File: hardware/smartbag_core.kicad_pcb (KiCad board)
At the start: 4 copper layers, 196 x 20 mm, 111 parts, among them J1 FFC optics, 12 way, J2 LiPo 3.7V 2000mAh + NTC, J3 Qi RX coil, J4 FFC FSR matrix, 24 way, J5 SWD debug, Q1 SI2302CDS-T1-GE3, U1 nRF54L15-QFAA-R, U11 BQ51013BRHLR, U2 Acconeer A121, U3 nPM1300-QEAA-R7, U4 BMI270, U5 DRV5032FBDBZR, U6 Acconeer A121, U7 CD74HC4067SM96, U8 TLV9064IPWR, U9 TLV9064IPWR, Y1 32 MHz Cl=8pF, Y2 24 MHz, Y3 24 MHz, Y4 32.768 kHz Cl=9pF

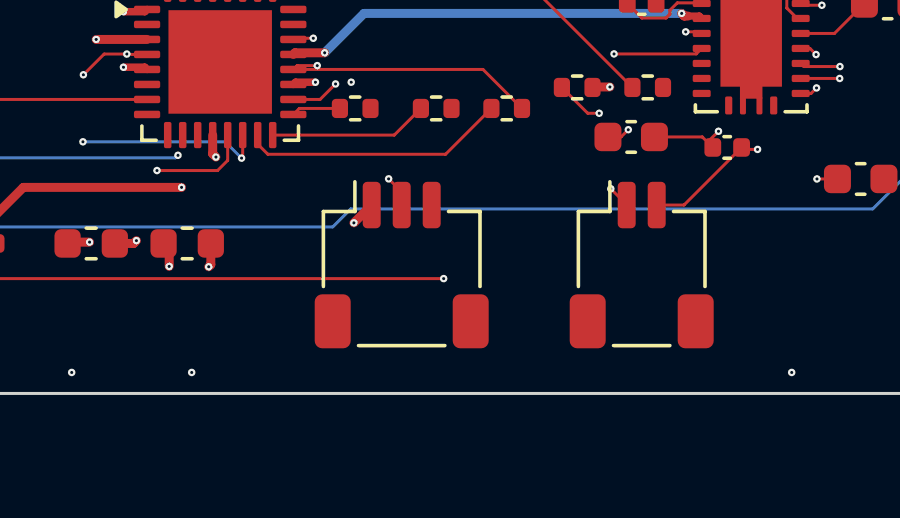
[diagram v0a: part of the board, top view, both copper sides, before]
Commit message: A battery you can order, and the coil comes out from under it
BT1 was the one line in the bill of materials that was not a part: a
4.2 x 58 x 148 mm semi-custom pouch, a shape derived from the insert
floor it had to fill. Nobody stocks that, so the design ended at "have a
cell made".

It is now Jauch LP523450JU — 950 mAh, 53.0 x 34.5 x 5.4 mm (5.8 after
cycling, and the pocket is cut to that), PCM, UN38.3, IEC62133-2, 507 in
stock at Digi-Key for $11.71. It brings its own 10k B=3435 thermistor on
pin 3 of a JST PHR-3 harness, which is exactly what nPM1300 wants and
what firmware/sb_power.c has been written against since the thermal
analysis asked for it.

⛔ AND THE PIN ORDER WAS WRONG. J2 was +, NTC, − — the order you choose
when you are drawing a connector rather than plugging one in. The harness
is 1 red (+), 2 black (−), 3 yellow (NTC), so the real cell would have
put its negative on the PMIC's thermistor input. Nothing here could have
caught it: every check asks whether a net reaches the pins it should, and
none of them knew what colour wire comes out of a pack that did not
exist. J2 is also a PH now rather than an SH — 2 A a contact instead of
1 A, which the note in bom.py had been asking for since the charge
current was first written down, and which is the housing the harness
comes with anyway.

⭐ THE CELL BEING 53 mm INSTEAD OF 148 DISSOLVED THE THERMAL FINDING.
thermal/budget.py has printed a cell near 60 °C against a 45 °C limit on
every run since it was written, and that number rested entirely on one
sentence in its docstring: the Qi coil sits directly under the LiPo. It
did, because a cell that filled the floor left nowhere else for the coil
to be. Now they sit side by side, 62 mm apart, and the heat would have to
cross 4493 K/W of foam to reach the cell when 23 K/W of air sits right
above the coil:

  cell   ~60 °C -> ~26 °C   (0.5% of the coil's rise)
  coil   ~60 °C, unchanged, and now the headline

⚠️ The finding moves rather than disappearing. A watt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
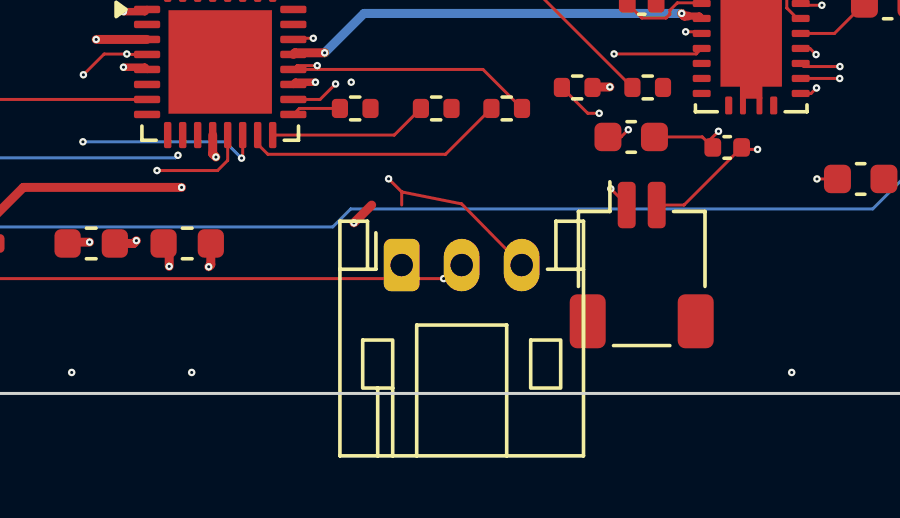
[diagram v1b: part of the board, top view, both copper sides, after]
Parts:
- J2: value LiPo 3.7V 2000mAh + NTC -> Jauch LP523450JU 950mAh; footprint Connector_JST:JST_SH_SM03B-SRSS-TB_1x03-1MP_P1.00mm_Horizontal -> Connector_JST:JST_PH_S3B-PH-K_1x03_P2.00mm_Horizontal
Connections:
- J2 pad 2: NTC -> GND
- J2 pad 3: GND -> NTC
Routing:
- net NTC: track 6.57 -> 11.5 mm

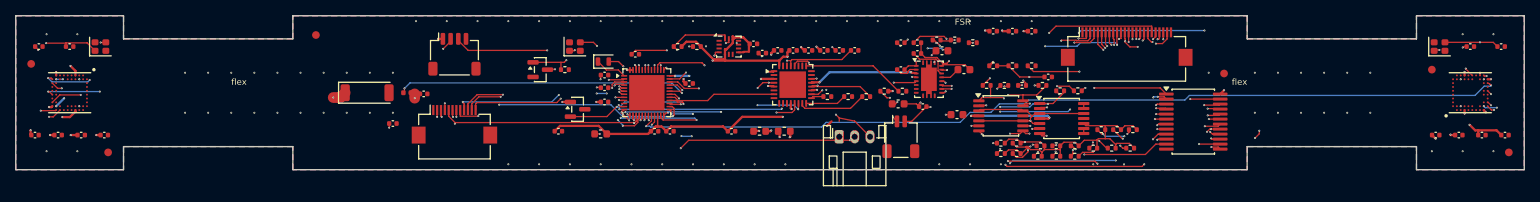
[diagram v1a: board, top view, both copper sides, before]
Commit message: set -e was decoration: every step was piped to tail
A crash inside specctra.py printed its traceback and the pipeline carried
straight on into fill, stitch and route. The board came out with 117
unconnected pads out of an import that had never happened, and reported
it as a normal run.

The cause is one line per script: `python3 ... | tail -1`. A pipeline's
exit status is the LAST command's, tail always succeeds, and `set -e`
therefore never saw anything fail. Five scripts now set pipefail.

⛔ AND THE CRASH ITSELF WAS TWO CLEANUP PASSES ON ONE BOARD. pcbnew's
GetTracks() is a live wrapper: once anything has been removed, it comes
back as a raw SWIG pointer that will not iterate — and on this machine
the second pass segfaulted rather than raising. Both cleanups now decide
against ONE snapshot and the caller removes once. That is not tidiness,
it is the only order that works.

The new cleanup is worth having on its own. Freerouting's optimiser
splits polylines and rounds the joins, leaving segments 0.0001 mm long —
a tenth of a micron — sitting at corners. Nine clearance violations on an
otherwise clean board were pairs of (a real track, one of those), because
a sliver still carries a full track width and so still has a clearance
envelope, pointing wherever the rounding chose.

⚠️ The threshold is 5 um and the number that justifies it is the track
WIDTH, not the fabricator's resolution: the narrowest track here is
100 um, so a 5 um segment lies entirely inside the copper it joins at
either end, twenty times over. Removing it cannot disconnect anything.
The first attempt used 1 um and left a 1.6 um stub behind, which DRC then
reported like any other track.

maze.py can now rip up as well as add. A board that came back with two
tracks 0.127 mm apart where the Power class asks for 0.15 was one it had
nothing to say about — it could only add copper, so it refused its own
routes for making a bad number worse and stopped. It now deletes the
shorter track of each clearance p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
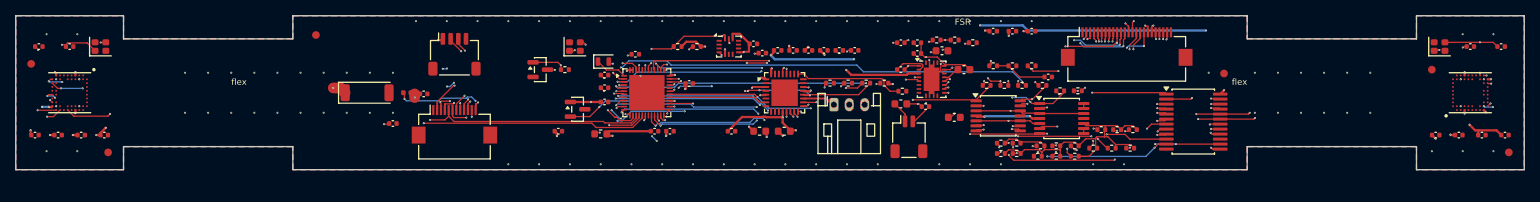
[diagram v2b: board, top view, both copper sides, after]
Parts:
- moved J2 4.23 mm to (218.3, 149.6)
- moved R2 1.78 mm to (217.8, 146.8)
- moved R3 1.75 mm to (220.2, 146.8)
- moved R4 1.75 mm to (222.5, 146.8)
- moved U3 1.48 mm to (211.9, 148.0)
- moved J3 1.05 mm to (228.1, 153.7)
- moved R5 1.05 mm to (224.8, 146.8)
- moved C88 0.49 mm to (233.9, 151.2)
- moved C80 0.35 mm to (227.0, 149.4)
- moved C81 0.35 mm to (230.2, 149.8)
- moved U11 0.35 mm to (231.0, 146.2)
- moved U8 0.35 mm to (239.7, 151.0)
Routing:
- net SPI_MISO: track 204.7 -> 80.8 mm, vias 8 -> 3
- net SPI_MOSI: track 211.5 -> 91.4 mm, vias 5 -> 4
- net MUX_EN_N: track 78.9 -> 0.00 mm, vias 2 -> 0
- net RADAR_EN: track 120.3 -> 77.0 mm, vias 6 -> 2
- net I2C_SCL: track 61.9 -> 80.9 mm, vias 8 -> 7
- net FSR_C7: track 24.2 -> 41.8 mm, vias 4 -> 3
- net FSR_C11: track 36.9 -> 53.0 mm, vias 3 -> 4
- net ADC0: track 62.8 -> 52.1 mm, vias 2 -> 3
- net XTAL32M_1: track 29.8 -> 19.1 mm
- net DECRF: track 19.6 -> 9.56 mm
- net VDD_1V8: track 253.4 -> 243.6 mm, vias 19 -> 21
- net CS_RADAR_L: track 76.0 -> 84.9 mm, vias 3 -> 4
- net FSR_C12: track 42.3 -> 51.2 mm, vias 3 -> 4
- net SWDIO: track 48.6 -> 39.8 mm, vias 3 -> 2
- net FSR_R1: track 32.3 -> 40.2 mm, vias 3 -> 4
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
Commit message: Fourteen ground balls per radar had no via
via_in_pad() dropped a via on every interior ball of the A121 except the
ground ones, and the reasoning for the exception was that ground reaches
the pour. An interior ball cannot reach the pour — that is the whole
argument the function's own docstring makes for the signal balls — and it
does not become able to because of what it is called.

Fourteen of each radar's interior balls are ground. Not one had a via:
the die's ground was tied to the plane by whatever copper squeezed
between balls on a 0.5 mm pitch. On a 60 GHz part with the antenna inside
the package, that is not a cosmetic complaint.

⚠️ IT COST ROUTING AND THE TRADE IS STILL RIGHT. Twenty-eight more vias
in the tightest area of the board, and freerouting came back with three
shorts and four clearance violations where it had had none. Together with
the JST PH the real cell brings — nearly twice the SH's area, in the part
of the board the SPI bus to the right radar has to cross — unconnected
went 3 -> 10 of about 500.

maze.py can now rip vias, not only tracks. The last violation standing
was a QI_ILIM via 0.0016 mm from a VDD_3V3 track, which nothing could act
on: the report parser read `Track [...]` and not `Via [...]`, so the tool
kept printing "0 ripped" against a violation it had just read. A via is
given length 0 so that when it is paired with a track the via is always
the one removed — a layer change is cheap to redo, four millimetres of
routed track is not.

Two smaller things from the same chase:
- shorts are ripped as well as clearances. A short is a clearance
  violation that went all the way, the repair is identical, and leaving
  them out meant the one violation that can destroy a board was the one
  nothing acted on.
- the offending item is matched by net and nearness rather than by an
  exact start point. DRC reports a point ON a track, which is its start
  only sometimes.

J2 also moved to x = -44: dimensions.py puts the cell at -62, so a
battery 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
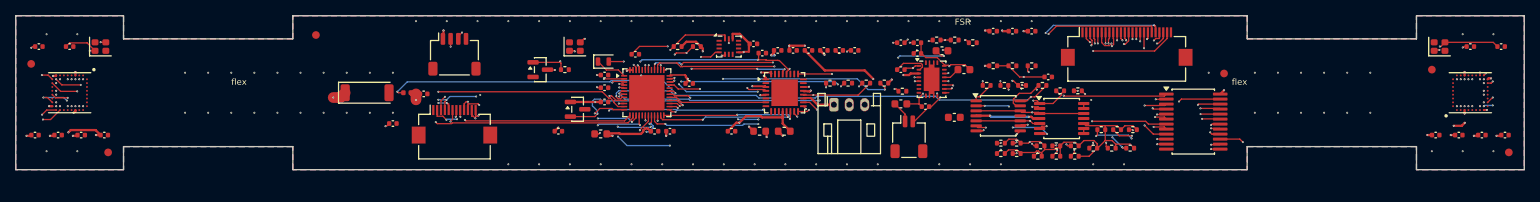
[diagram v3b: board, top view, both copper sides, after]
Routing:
- net SPI_MISO: track 80.8 -> 210.3 mm, vias 3 -> 8
- net SPI_SCK: track 200.7 -> 94.0 mm, vias 7 -> 3
- net MUX_EN_N: track 0.00 -> 87.1 mm, vias 0 -> 2
- net RADAR_EN: track 77.0 -> 0.00 mm, vias 2 -> 0
- net FSR_C7: track 41.8 -> 23.6 mm, vias 3 -> 4
- net DECRF: track 9.56 -> 26.9 mm
- net FSR_C11: track 53.0 -> 39.0 mm, vias 4 -> 3
- net VDD_3V3: track 327.4 -> 338.6 mm, vias 32 -> 33
- net VDD_1V8: track 243.6 -> 254.2 mm, vias 21 -> 20
- net ADC1: track 71.2 -> 60.7 mm, vias 7 -> 4
- net CS_RADAR_L: track 84.9 -> 75.3 mm, vias 4 -> 3
- net FSR_C12: track 51.2 -> 42.8 mm, vias 4 -> 3
- net QI_RECT: track 8.22 -> 0.00 mm, vias 2 -> 0
- net I2C_SCL: track 80.9 -> 72.7 mm, vias 7 -> 6
- net SPI_MOSI: track 91.4 -> 83.3 mm, vias 4 -> 5
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
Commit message: Flex tails 14 mm -> 17 mm, and the optimiser's speed-up is a trap
The tails were widened from 8 to 14 mm once already, and the argument has
not changed: bend radius is a function of THICKNESS, not width, so a
wider tail folds exactly as tightly and just carries more copper across
the fold. 14 was still the bottleneck once the real cell brought a JST PH
twice the SH's area and the A121's fourteen interior ground balls got the
vias they needed — the SPI bus to the right radar was the first thing the
router gave up on, again. 17 and not 20 because a millimetre and a half
of polyimide either side of the copper is what keeps a fold from tearing
at the edge of a track.

⛔ AND THE OPTIMISER'S OWN LOG SAYS IT RUNS ON ONE THREAD. On the wider
board that phase ran over two hours after an auto-route that had finished
in eighteen minutes, so handing it the machine's other eight cores looks
like the whole fix. Freerouting's answer to -mt 8 is a warning in its own
log: "Multi-threaded route optimization is broken and it is known to
generate clearance violations." So the stall is paid rather than solved —
it costs wall-clock and nothing else, because the optimiser trims vias
and length and does not change connectivity. It has to be waited out only
because the session file is written at the very end.

Co-Authored-By: Claude Opus 5 <noreply@anthropic.com>
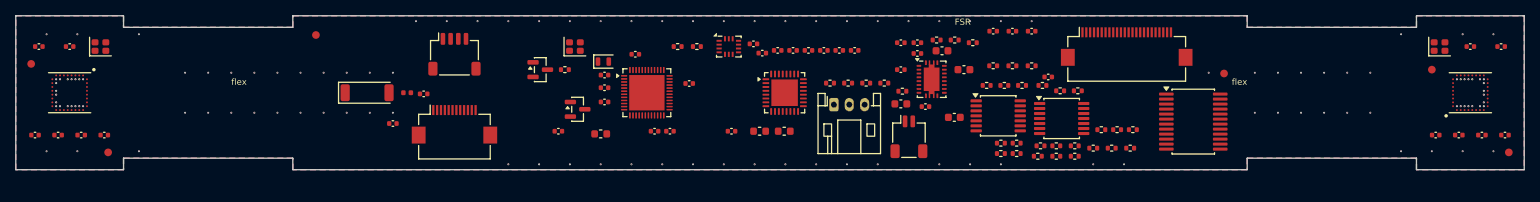
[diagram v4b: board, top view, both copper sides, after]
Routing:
- net VDD_3V3: track 338.6 -> 0.00 mm, vias 33 -> 0
- net VDD_1V8: track 254.2 -> 0.00 mm, vias 20 -> 6
- net SPI_MISO: track 210.3 -> 0.00 mm, vias 8 -> 0
- net RADAR_IRQ_R: track 126.4 -> 0.00 mm, vias 3 -> 0
- net CS_RADAR_R: track 119.7 -> 0.00 mm, vias 4 -> 1
- net SPI_SCK: track 94.0 -> 0.00 mm, vias 3 -> 0
- net MUX_S2: track 91.7 -> 0.00 mm, vias 4 -> 0
- net MUX_EN_N: track 87.1 -> 0.00 mm, vias 2 -> 0
- net MUX_S0: track 84.5 -> 0.00 mm, vias 4 -> 0
- net MUX_S1: track 84.5 -> 0.00 mm, vias 4 -> 0
- net SPI_MOSI: track 83.3 -> 0.00 mm, vias 5 -> 0
- net RADAR_IRQ_L: track 80.9 -> 0.00 mm, vias 3 -> 0
- net VREF: track 79.4 -> 0.00 mm, vias 4 -> 0
- net MUX_S3: track 78.9 -> 0.00 mm, vias 2 -> 0
- net I2C_SDA: track 77.1 -> 0.00 mm, vias 4 -> 0
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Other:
- outline, holes or cut-outs redrawn

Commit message: A fanout via per pin: 10 unconnected -> 1
Forty-eight pins escaping on a single layer was the bottleneck all along,
and it stayed invisible because it never produced a wrong answer — only a
router that gave up. U1 is a QFN48 on a 0.4 mm pitch with thirty-five
signals to get out; without a fanout each one travels on F.Cu until it
finds room to drop, so the pins facing away from their destination cross
the whole package on the board's most congested layer.

qfn_fanout() puts a via 0.35 mm outside every signal pin of U1, U3 and
U7, outward along the pad's own normal so it never lands between two
pins. It is what a person would draw and the standard escape for a
fine-pitch QFN: one via per signal, and the router starts with three
layers instead of one.

  wider flex tails (14 -> 17 mm)              10 -> 10
  ground vias on the radars' interior balls   10 -> 10
  a fanout via per QFN signal pin             10 ->  4
  supply pins in the fanout too                4 ->  1

⚠️ The first two look like they did nothing and neither was wasted — the
tails carry the SPI bus the fanout then had somewhere to put, and the
ground vias are an RF requirement rather than a routing one. What the
table shows is that changing one thing at a time is the only way to learn
which one was the constraint.

⛔ SUPPLY PINS WERE EXCLUDED FROM THE FANOUT AND THAT COST THE LAST THREE.
A power pin is not special in a row of pins; it needs an escape like any
other. Ground still is special, and still skipped: a ground pin under a
QFN reaches the plane through the exposed pad's own thermal vias.

Three more things the fabrication package needed:

- nine dangling fanout vias. The router does not take every escape it is
  offered, and what it leaves is a drill hit somebody pays for. maze.py
  --tidy removes vias DRC reports as connected on one layer. Vias only:
  a dangling TRACK is usually the near end of a connection that did not
  finish, and deleting it removes the evidence of what is missing.
- the ba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
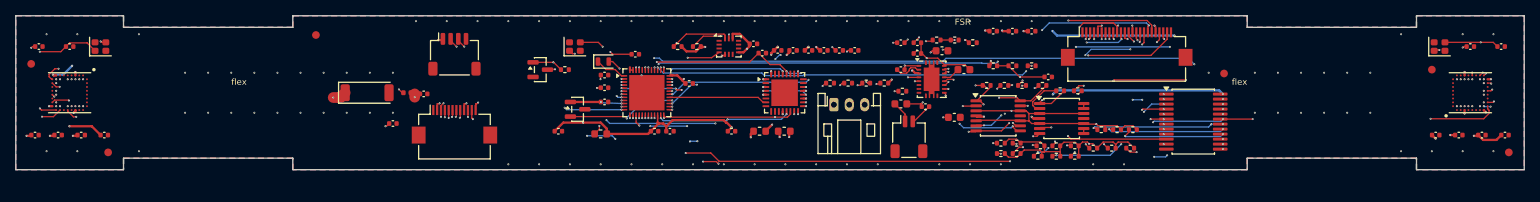
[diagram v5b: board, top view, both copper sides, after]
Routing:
- net VDD_3V3: track 0.00 -> 340.1 mm, vias 0 -> 29
- net VDD_1V8: track 0.00 -> 250.5 mm, vias 6 -> 21
- net SPI_SCK: track 0.00 -> 211.9 mm, vias 0 -> 8
- net SPI_MOSI: track 0.00 -> 209.0 mm, vias 0 -> 6
- net SPI_MISO: track 0.00 -> 204.0 mm, vias 0 -> 7
- net RADAR_EN: track 0.00 -> 199.2 mm, vias 0 -> 7
- net RADAR_IRQ_R: track 0.00 -> 120.3 mm, vias 0 -> 4
- net CS_RADAR_R: track 0.00 -> 117.0 mm, vias 1 -> 3
- net MUX_S2: track 0.00 -> 84.7 mm, vias 0 -> 2
- net VREF: track 0.00 -> 81.7 mm, vias 0 -> 4
- net CS_RADAR_L: track 0.00 -> 79.4 mm, vias 1 -> 2
- net RADAR_IRQ_L: track 0.00 -> 79.0 mm, vias 0 -> 2
- net MUX_EN_N: track 0.00 -> 78.7 mm, vias 0 -> 4
- net MUX_S3: track 0.00 -> 78.7 mm, vias 0 -> 2
- net MUX_S1: track 0.00 -> 77.5 mm, vias 0 -> 2
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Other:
- board text added: "17 mm flex tails: min bend radius 2 mm (10x thickness)"
- board text added: "A121: antenna in package, no 60 GHz copper here"
- board text added: "SMARTBAG CORE v0.3"
- board text added: "U1 nRF54L15 U2/U6 A121 60 GHz U3 nPM1300"
- board text added: "U4 BMI270 IMU U5 zip Hall U11 BQ51013B Qi"
- board text added: "rigid FR4 islands 0.6 mm on 2L polyimide flex, 4 copper layers"
- board text added: "tagless inventory - 4L rigid-flex"
- board text removed: "8 mm flex tails: min bend radius 12 mm (10x thickness)"
- board text removed: "SMARTBAG CORE v0.2"
- board text removed: "U1 SoC+NPU U2 60 GHz radar U3 PMIC"
- board text removed: "U2/U6 A121: 60 GHz radar, antenna in package"
- board text removed: "U4 6-axis IMU U5 zip Hall Y1 32 MHz"
- board text removed: "rigid FR4 islands 0.6 mm on 2L polyimide flex"
- board text removed: "tagless inventory - 2L rigid-flex"

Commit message: A bill of materials you can put in a basket
23 named parts, each with a manufacturer number whose package was
measured against its own datasheet — and none of that puts anything in a
cart. tools/order.py writes what a distributor takes: part number and
quantity, for a BUILD rather than for a board, because five prototypes of
a design with two radars on it is ten radars and the commonest way to be
short on assembly day is to have ordered one board's worth of something
that appears twice.

Trying to order found two parts that do not exist to order, the same way
the battery was found — by looking for a basket rather than for a
datasheet:

- U10 was "VL53L1X", which is the family. The orderable chip is
  VL53L1CXV0FY/1, $6.63.
- L_COIL was Würth 760308103305, which is not in Digi-Key's catalogue at
  all. 760308103202 is, and it fits the CAD exactly — 48 mm across, the
  24 mm radius cad/bag_and_insert.py has always drawn, 1.0 mm tall in a
  1.4 mm recess.

⛔ AND THE COIL CHANGED THE CIRCUIT. 12 µH instead of 8.8 moves both
resonant capacitors — Cs 270 → 220 nF, Cd 2.7 → 2.2 nF — and NOTHING
JOINED the calculation to the board. qi_resonance.py derived the values
and netlist.py had numbers typed into two capacitors; swapping the coil
would have left a tank tuned for a part nobody could buy, silently.
tools/check.py now compares the fitted values against the computation and
the BOM's coil against the one the computation used.

⚠️ Prices carry the date they were taken. $652.61 covers the twelve lines
that dominate the cost, at five boards; the fifteen left are 0402-class
commodity. A number in a repository does not go out of stock on its own,
which is why the deliverable is an upload file rather than a price list.

⚠️ And two lines decide the schedule rather than the cost: the coil showed
ZERO stock at Digi-Key, so it is the line to order first, and the cell is
a lithium pouch that ships under UN38.3 with couriers that may refuse it
by air.

The passives are a specificatio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
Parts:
- C80: value 270n C0G (Cs) -> 220n C0G (Cs)
- C81: value 2n7 C0G (Cd) -> 2n2 C0G (Cd)
